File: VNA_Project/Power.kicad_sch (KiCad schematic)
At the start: 17 parts, among them J2 Jack-DC, U1 AP7375, U100 HT7533-1

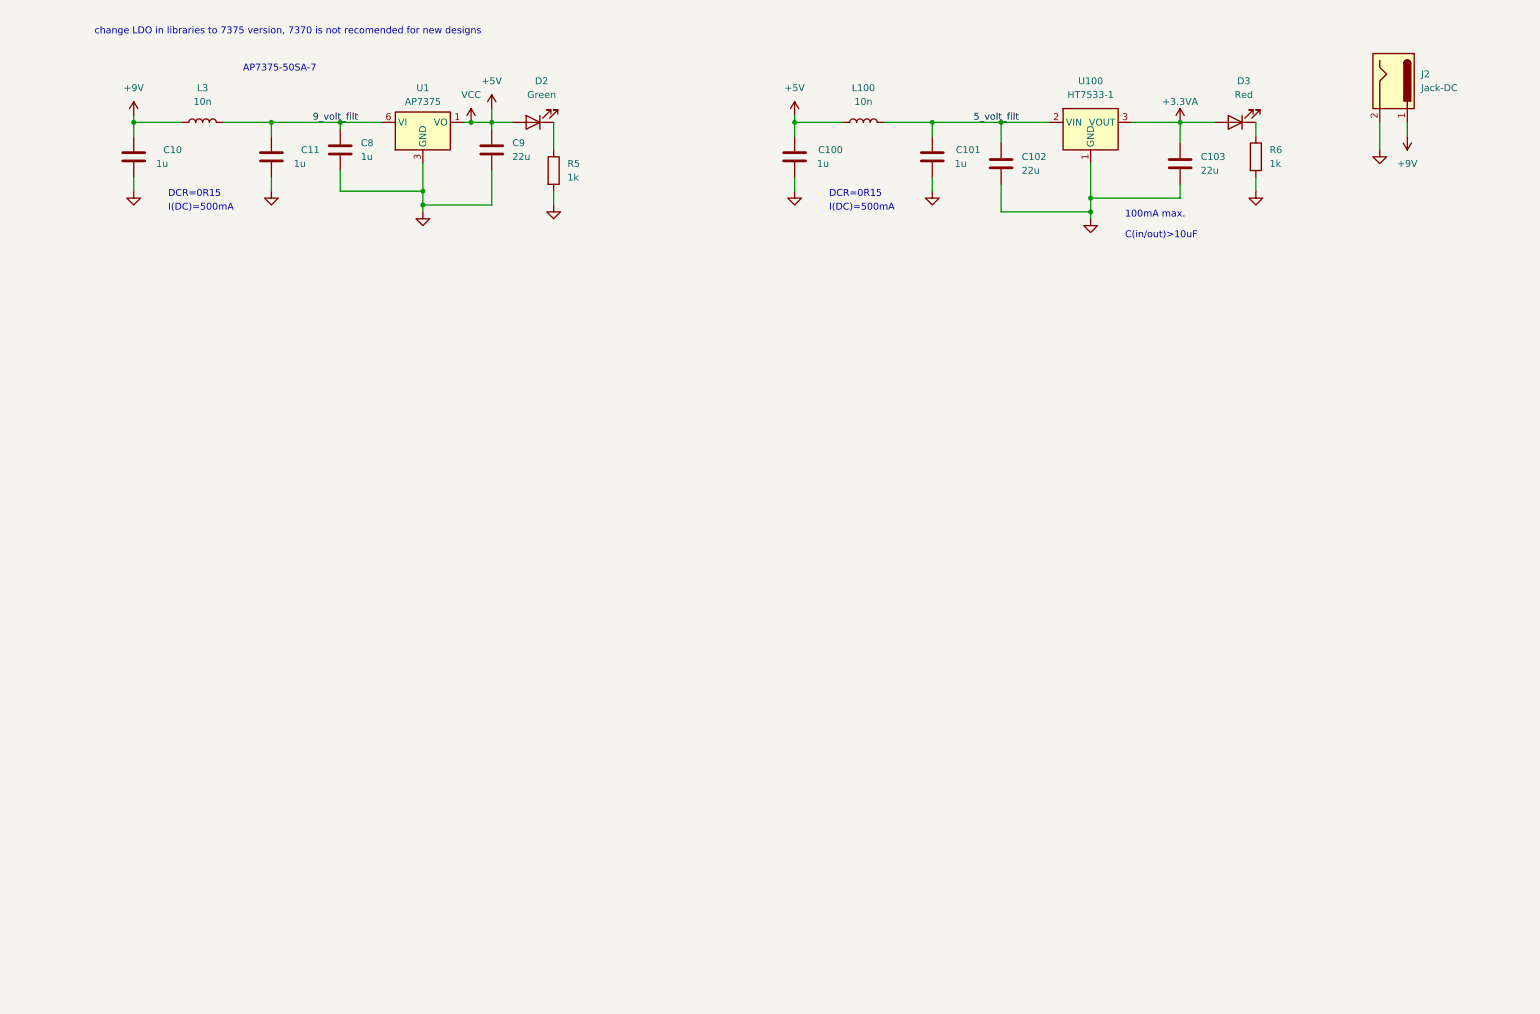
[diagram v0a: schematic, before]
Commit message: Added ESP32 MCU design
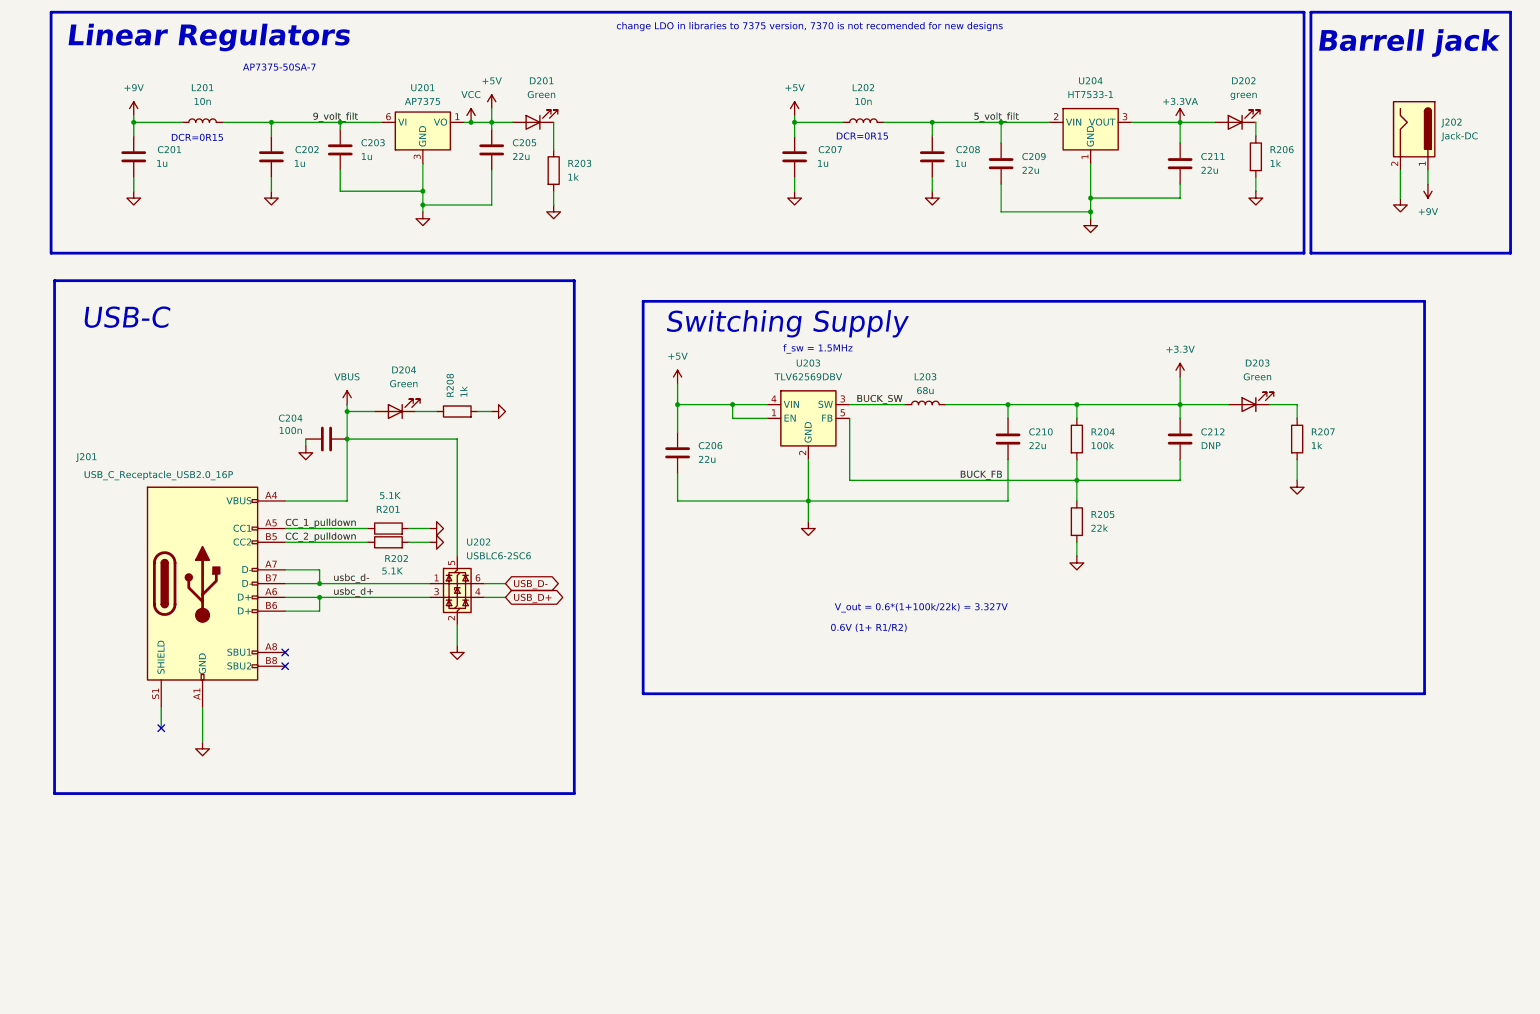
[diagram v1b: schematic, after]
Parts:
- added C204: 100n, Capacitor_SMD:C_0402_1005Metric_Pad0.74x0.62mm_HandSolder, symbol Device:C
- added C206, C210: 22u, Capacitor_SMD:C_0603_1608Metric_Pad1.08x0.95mm_HandSolder, symbol Device:C
- added C212: DNP, Capacitor_SMD:C_0402_1005Metric_Pad0.74x0.62mm_HandSolder, symbol Device:C
- added D203: Green, LED_SMD:LED_0402_1005Metric_Pad0.77x0.64mm_HandSolder, symbol Device:LED
- added D204: Green, symbol Device:LED
- added J201: USB_C_Receptacle_USB2.0_16P, Connector_USB:USB_C_Receptacle_G-Switch_GT-USB-7010ASV, symbol Connector:USB_C_Receptacle_USB2.0_16P
- added L203: 68u, Inductor_SMD:L_0603_1608Metric_Pad1.05x0.95mm_HandSolder, symbol Device:L
- added R201, R202: 5.1K, Resistor_SMD:R_0402_1005Metric_Pad0.72x0.64mm_HandSolder, symbol Device:R
- added R204: 100k, Resistor_SMD:R_0402_1005Metric_Pad0.72x0.64mm_HandSolder, symbol Device:R
- added R205: 22k, Resistor_SMD:R_0402_1005Metric_Pad0.72x0.64mm_HandSolder, symbol Device:R
- added R207: 1k, Resistor_SMD:R_0402_1005Metric_Pad0.72x0.64mm_HandSolder, symbol Device:R
- added R208: 1k, symbol Device:R
- added U202: USBLC6-2SC6, Package_TO_SOT_SMD:SOT-23-6, symbol Power_Protection:USBLC6-2SC6
- added U203: TLV62569DBV, Package_TO_SOT_SMD:SOT-23-5, symbol Regulator_Switching:TLV62569DBV
- D202: renamed from D3; value Red -> green
- renumbered C10 to C201, C11 to C202, C8 to C203, C9 to C205, C100 to C207, C101 to C208, C102 to C209, C103 to C211, D2 to D201, J2 to J202, L3 to L201, L100 to L202, R5 to R203, R6 to R206, U1 to U201, U100 to U204
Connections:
- net +5V: now also C206.1, U203.1 (EN), U203.4 (VIN)
- net GND: now also C204.1, C206.2, C210.2, J201.A1 (GND), J201.A12 (GND), J201.B1 (GND), J201.B12 (GND), R201.2, R202.2, R205.2, R207.2, R208.2, U202.2 (GND), U203.2 (GND)
- new net: D203.1 (K), R207.1
- new net: D204.1 (K), R208.1
- new net +3.3V: C210.1, C212.1, D203.2 (A), L203.2, R204.1
- new net BUCK_FB: C212.2, R204.2, R205.1, U203.5 (FB)
- new net BUCK_SW: L203.1, U203.3 (SW)
- new net CC_1_pulldown: J201.A5 (CC1), R201.1
- new net CC_2_pulldown: J201.B5 (CC2), R202.1
- new net USB_D+: U202.4 (I/O2)
- new net USB_D-: U202.6 (I/O1)
- new net VBUS: C204.2, D204.2 (A), J201.A4 (VBUS), J201.A9 (VBUS), J201.B4 (VBUS), J201.B9 (VBUS), U202.5 (VBUS)
- new net usbc_d+: J201.A6 (D+), J201.B6 (D+), U202.3 (I/O2)
- new net usbc_d-: J201.A7 (D-), J201.B7 (D-), U202.1 (I/O1)
- no-connect marks 0 -> 3
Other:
- note added: "0.6V (1+ R1/R2)"
- note added: "Barrell jack"
- note added: "Linear Regulators"
- note added: "Switching Supply"
- note added: "USB-C"
- note added: "V_out = 0.6*(1+100k/22k) = 3.327V"
- note added: "f_sw = 1.5MHz"
- note removed: "100mA max."
- note removed: "C(in/out)>10uF"
- note removed: "I(DC)=500mA"
- moved on the sheet: J202

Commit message: Changing from a ESP32 S3 to STM32 H7 high performance MCU for USB HS and ETH capabilities
Changing from a ESP32 S3 to STM32 H7 high performance MCU for USB HS and ETH capabilities
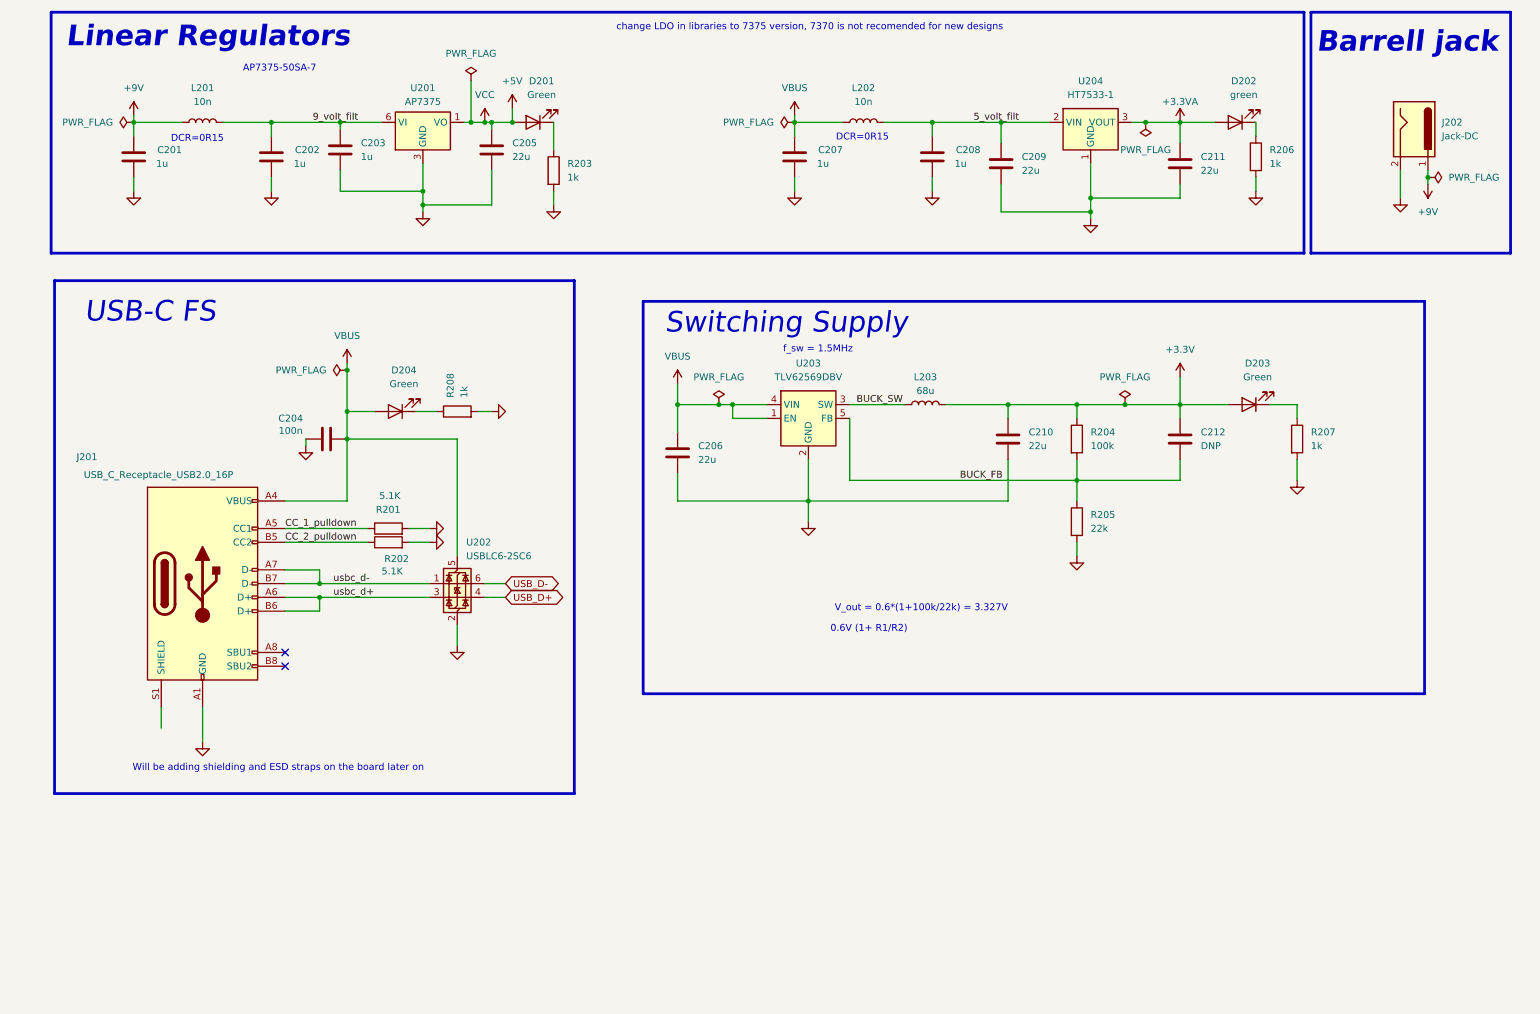
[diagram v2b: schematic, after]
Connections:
- net +5V: no longer C206.1, C207.1, L202.1, U203.1 (EN), U203.4 (VIN)
- net VBUS: now also C206.1, C207.1, L202.1, U203.1 (EN), U203.4 (VIN)
- no-connect marks 3 -> 2
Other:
- note added: "USB-C FS"
- note added: "Will be adding shielding and ESD straps on the board later on"
- note removed: "USB-C"

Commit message: minor changes
minor changes
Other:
- note added: "Use X7R Caps"
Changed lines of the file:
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@@
+		)
+	)
+	(text "Use X7R Caps \n"
+		(exclude_from_sim no)
+		(at 206.502 15.24 0)
+		(effects
+			(font
+				(size 1.27 1.27)
+			)
 		)
 	)

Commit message: Eth done
Eth done
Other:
- moved on the sheet: C206, C210, C212, D203, L203, R204, R205, R207, U203

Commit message: adc
adc
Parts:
- removed C201, C202: 1u, Capacitor_SMD:C_0603_1608Metric, symbol Device:C
- removed L201: 10n, Inductor_SMD:L_0402_1005Metric, symbol Device:L
- added C25, C26: 1u, symbol Device:C
- added D1: Green, symbol Device:LED
- added R29: 1k, symbol Device:R
- added U6: MIC5501-3.0YM5, Package_TO_SOT_SMD:SOT-23-5, symbol Regulator_Linear:MIC5501-3.0YM5
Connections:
- net 9_volt_filt is gone; now on net +9V: C203.1, U201.6 (VI)
- net GND: now also C25.2, C26.2, R29.2, U6.2 (GND)
- net VBUS: now also C25.1, U6.1 (VIN), U6.3 (EN)
- new net: D1.1 (K), R29.1
- new net +3V0: C26.1, D1.2 (A), U6.5 (VOUT)
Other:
- moved on the sheet: C203, C204, C205, C206, C207, C208, C209, C210, C211, C212, D201, D202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

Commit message: DAC
DAC
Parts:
- D202: value green -> Green
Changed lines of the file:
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@@
+	(wire
+		(pts
+			(xy 60.96 36.83) (xy 60.96 38.1)
+		)
+		(stroke
+			(width 0)
+			(type default)
+		)
+	)
 	(wire
 		(pts
@@
 			)
 		)
-		(property "Value" "green"
+		(property "Value" "Green"
 			(at 176.8475 33.02 0)
 			(effects
@@
 	(symbol
 		(lib_id "power:VCC")
-		(at 60.96 38.1 0)
+		(at 60.96 36.83 0)
 		(unit 1)
 		(exclude_from_sim no)
@@
 		(fields_autoplaced yes)
 		(property "Reference" "#PWR0210"
-			(at 60.96 41.91 0)
+			(at 60.96 40.64 0)
 			(effects
 				(font
@@
 		)
 		(property "Value" "VCC"
-			(at 60.96 33.02 0)
+			(at 60.96 31.75 0)
 			(effects
 				(font
@@
 		)
 		(property "Footprint" ""
-			(at 60.96 38.1 0)
+			(at 60.96 36.83 0)
 			(effects
 				(font
@@
 		)
 		(property "Datasheet" ""
-			(at 60.96 38.1 0)
+			(at 60.96 36.83 0)
 			(effects
 				(font
@@
 		)
 		(property "Description" "Power symbol creates a global label with name \"VCC\""
-			(at 60.96 38.1 0)
-			(effects
-				(font
+			(at 60.96 36.83 0)
+			(effects
+				(font
